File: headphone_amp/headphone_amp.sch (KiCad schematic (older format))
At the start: 40 parts, among them J1 Molex_SL_01x02_Male, J2 Molex_SL_01x02_Male, J3 Molex_SL_01x03_Male, J4 Molex_SL_01x03_Male, Q1 PZTA42, Q2 PZTA92, Q3 PZTA42, Q4 PZTA92, U1 NE5532

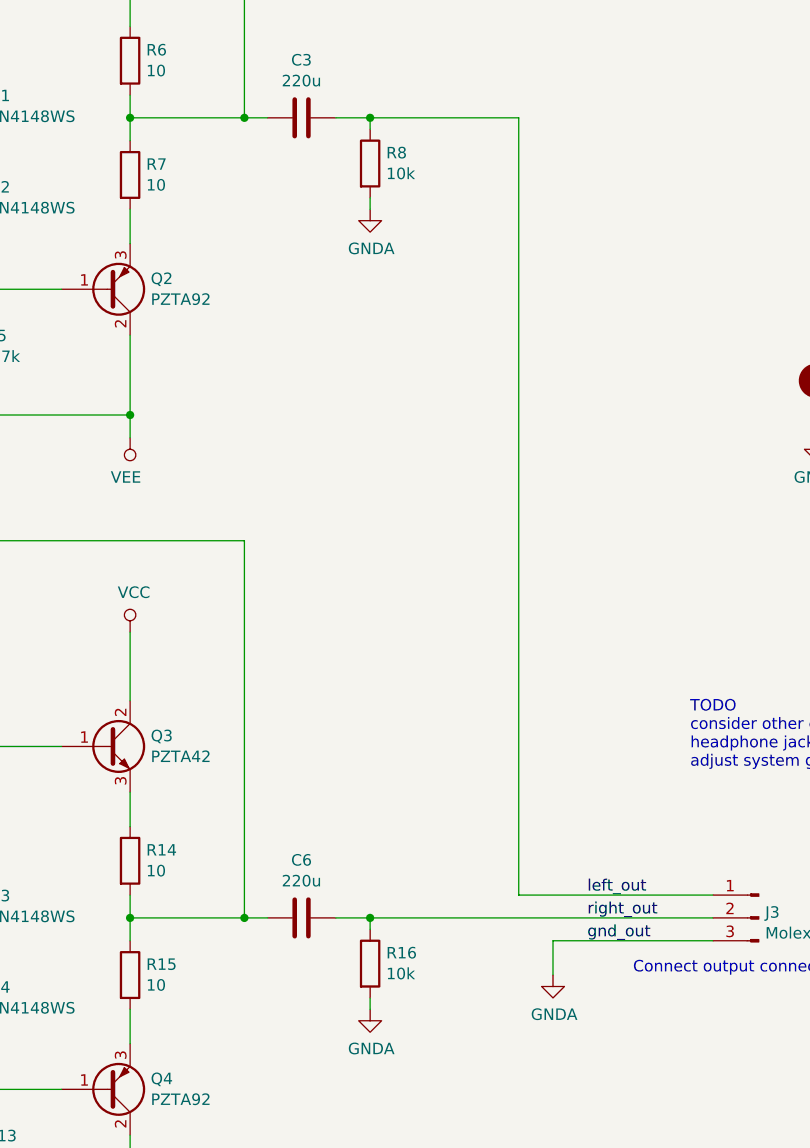
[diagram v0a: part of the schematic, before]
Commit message: update output cap footprint and bleeder resistor
- update output cap footprint (20mm height vs 25mm to match actual part)
- increase bleeder resistor value to 22k from 10k, to decrease corner
frequency
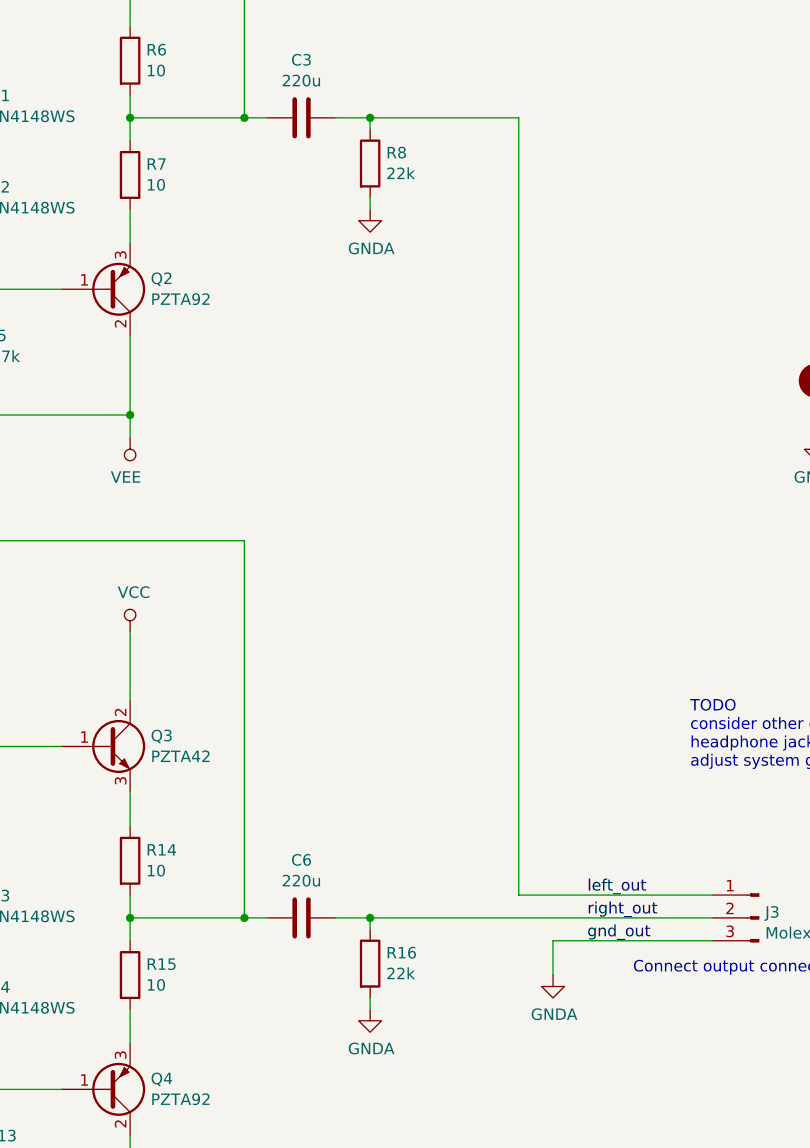
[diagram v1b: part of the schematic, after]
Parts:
- C3, C6: footprint Capacitor_THT:C_Radial_D12.5mm_H25.0mm_P5.00mm -> Capacitor_THT:C_Radial_D12.5mm_H20.0mm_P5.00mm
- R16, R8: value 10k -> 22k
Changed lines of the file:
@@
 F 0 "C3" V 5798 2550 50  0000 C CNN
 F 1 "220u" V 5889 2550 50  0000 C CNN
-F 2 "Capacitor_THT:C_Radial_D12.5mm_H25.0mm_P5.00mm" H 6088 2400 50  0001 C CNN
+F 2 "Capacitor_THT:C_Radial_D12.5mm_H20.0mm_P5.00mm" H 6088 2400 50  0001 C CNN
 F 3 "http://nichicon-us.com/english/products/pdfs/e-uvp.pdf" H 6050 2550 50  0001 C CNN
 F 4 "Nichicon" H 6050 2550 50  0001 C CNN "Manufacturer"
@@
 F 0 "C6" V 5798 6050 50  0000 C CNN
 F 1 "220u" V 5889 6050 50  0000 C CNN
-F 2 "Capacitor_THT:C_Radial_D12.5mm_H25.0mm_P5.00mm" H 6088 5900 50  0001 C CNN
+F 2 "Capacitor_THT:C_Radial_D12.5mm_H20.0mm_P5.00mm" H 6088 5900 50  0001 C CNN
 F 3 "http://nichicon-us.com/english/products/pdfs/e-uvp.pdf" H 6050 6050 50  0001 C CNN
 F 4 "Nichicon" H 6050 6050 50  0001 C CNN "Manufacturer"
@@
 P 6350 6250
 F 0 "R16" H 6420 6296 50  0000 L CNN
-F 1 "10k" H 6420 6205 50  0000 L CNN
+F 1 "22k" H 6420 6205 50  0000 L CNN
 F 2 "Resistor_SMD:R_0603_1608Metric_Pad1.05x0.95mm_HandSolder" V 6280 6250 50  0001 C CNN
 F 3 "~" H 6350 6250 50  0001 C CNN
@@
 P 6350 2750
 F 0 "R8" H 6420 2796 50  0000 L CNN
-F 1 "10k" H 6420 2705 50  0000 L CNN
+F 1 "22k" H 6420 2705 50  0000 L CNN
 F 2 "Resistor_SMD:R_0603_1608Metric_Pad1.05x0.95mm_HandSolder" V 6280 2750 50  0001 C CNN
 F 3 "~" H 6350 2750 50  0001 C CNN

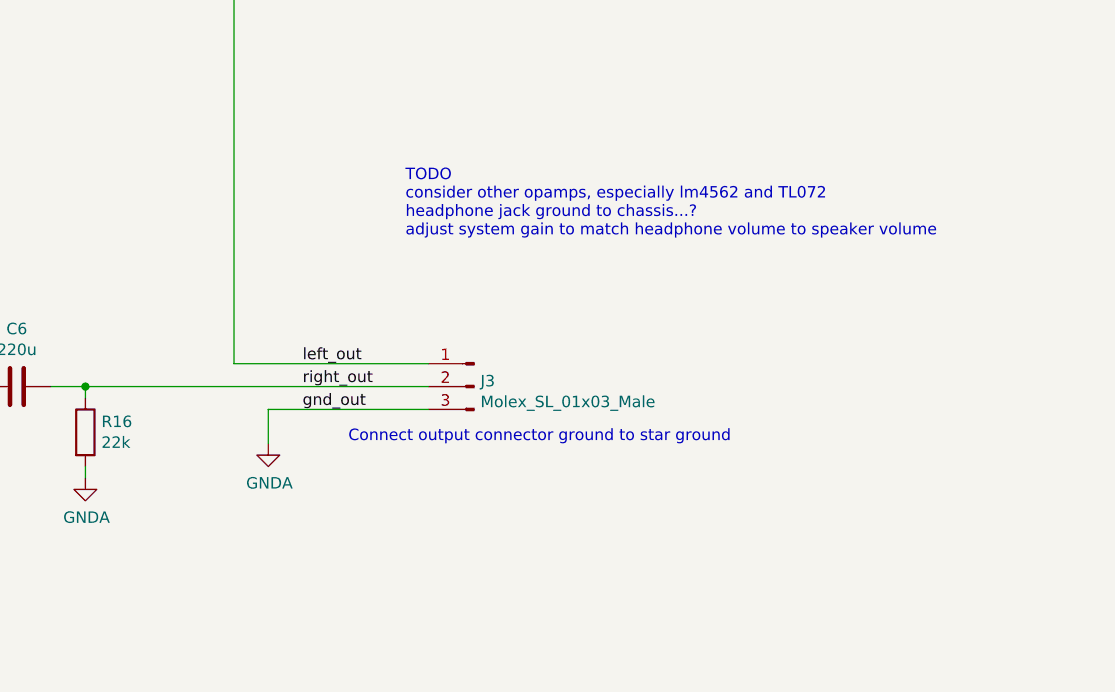
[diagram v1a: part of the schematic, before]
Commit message: connect output jack ground to star point with net tie
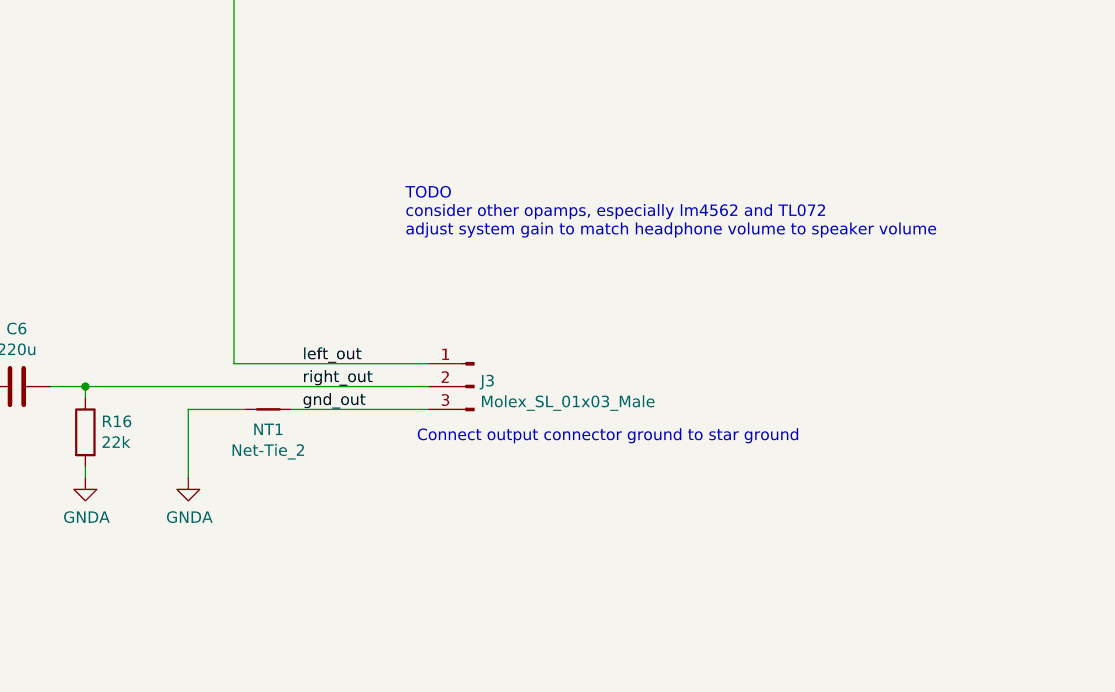
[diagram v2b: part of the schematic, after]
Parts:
- added NT1: Net-Tie_2, NetTie:NetTie-2_SMD_Pad2.0mm, symbol Device:Net-Tie_2
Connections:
- net GNDA: now also NT1.1; no longer J3.3 (Pin_3)
- new net gnd_out: J3.3 (Pin_3), NT1.2
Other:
- note added: "TODO\nconsider other opamps, especially lm4562 and TL072\nadjust system gain to match headphone volume to speaker volume"
- note removed: "TODO\nconsider other opamps, especially lm4562 and TL072\nheadphone jack ground to chassis...?\nadjust system gain to match headphone volume to speaker volume"
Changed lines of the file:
@@
 Connection ~ 1500 7350
 Text Notes 7750 5400 0    50   ~ 0
-TODO\nconsider other opamps, especially lm4562 and TL072\nheadphone jack ground to chassis...?\nadjust system gain to match headphone volume to speaker volume
+TODO\nconsider other opamps, especially lm4562 and TL072\nadjust system gain to match headphone volume to speaker volume
 $Comp
 L Connector_gkeeth:Molex_SL_01x02_Male J1
@@
 L power:GNDA #PWR0115
 U 1 1 5D92A4FE
-P 7150 6300
-F 0 "#PWR0115" H 7150 6050 50  0001 C CNN
-F 1 "GNDA" H 7155 6127 50  0000 C CNN
-F 2 "" H 7150 6300 50  0001 C CNN
-F 3 "" H 7150 6300 50  0001 C CNN
-	1    7150 6300
-	1    0    0    -1
-$EndComp
-Wire Wire Line
-	7150 6300 7150 6150
-Wire Wire Line
-	7150 6150 7850 6150
+P 6800 6450
+F 0 "#PWR0115" H 6800 6200 50  0001 C CNN
+F 1 "GNDA" H 6805 6277 50  0000 C CNN
+F 2 "" H 6800 6450 50  0001 C CNN
+F 3 "" H 6800 6450 50  0001 C CNN
+	1    6800 6450
+	1    0    0    -1
+$EndComp
 $Comp
 L Mechanical:MountingHole_Pad H1
@@
 Text Label 7300 6150 0    50   ~ 0
 gnd_out
-Text Notes 7500 6300 0    50   ~ 0
+Text Notes 7800 6300 0    50   ~ 0
 Connect output connector ground to star ground
 $Comp
@@
 $EndComp
 $Comp
-L power:GNDA #PWR?
+L power:GNDA #PWR0118
 U 1 1 5D8D030E
 P 6350 2950
-F 0 "#PWR?" H 6350 2700 50  0001 C CNN
+F 0 "#PWR0118" H 6350 2700 50  0001 C CNN
 F 1 "GNDA" H 6355 2777 50  0000 C CNN
 F 2 "" H 6350 2950 50  0001 C CNN
@@
 	6350 2550 7000 2550
 $Comp
-L power:GNDA #PWR?
+L power:GNDA #PWR0119
 U 1 1 5D8DF1C2
 P 6350 6450
-F 0 "#PWR?" H 6350 6200 50  0001 C CNN
+F 0 "#PWR0119" H 6350 6200 50  0001 C CNN
 F 1 "GNDA" H 6355 6277 50  0000 C CNN
 F 2 "" H 6350 6450 50  0001 C CNN
@@
 	1    0    0    -1
 $EndComp
+$Comp
+L Device:Net-Tie_2 NT1
+U 1 1 5D95037D
+P 7150 6150
+F 0 "NT1" H 7150 6061 50  0000 C CNN
+F 1 "Net-Tie_2" H 7150 5970 50  0000 C CNN
+F 2 "NetTie:NetTie-2_SMD_Pad2.0mm" H 7150 6150 50  0001 C CNN
+F 3 "~" H 7150 6150 50  0001 C CNN
+	1    7150 6150
+	1    0    0    -1
+$EndComp
+Wire Wire Line
+	7250 6150 7850 6150
+Wire Wire Line
+	6800 6450 6800 6150
+Wire Wire Line
+	6800 6150 7050 6150
 $EndSCHEMATC

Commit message: change to M3 mounting holes
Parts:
- H1, H2: footprint MountingHole:MountingHole_4.5mm_Pad -> MountingHole:MountingHole_3.2mm_M3_Pad
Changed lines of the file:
@@
 F 0 "H1" H 8400 3799 50  0000 L CNN
 F 1 "MountingHole_Pad" H 8400 3708 50  0000 L CNN
-F 2 "MountingHole:MountingHole_4.5mm_Pad" H 8300 3750 50  0001 C CNN
+F 2 "MountingHole:MountingHole_3.2mm_M3_Pad" H 8300 3750 50  0001 C CNN
 F 3 "~" H 8300 3750 50  0001 C CNN
 	1    8300 3750
@@
 F 0 "H2" H 9450 3799 50  0000 L CNN
 F 1 "MountingHole_Pad" H 9450 3708 50  0000 L CNN
-F 2 "MountingHole:MountingHole_4.5mm_Pad" H 9350 3750 50  0001 C CNN
+F 2 "MountingHole:MountingHole_3.2mm_M3_Pad" H 9350 3750 50  0001 C CNN
 F 3 "~" H 9350 3750 50  0001 C CNN
 	1    9350 3750

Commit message: enter all BOM info
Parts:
- C1, C2, C4, C5: Dielectric (none) -> C0G/NP0; Distributor (none) -> Mouser; Distributor PN (none) -> 80-C0603C220J5G7411; Manufacturer (none) -> KEMET; Manufacturer PN (none) -> C0603C220J5GAC7411; URL (none) -> https://www.mouser.com/ProductDetail/80-C0603C220J5G7411; Unit Price (none) -> 0.23
- D1, D2, D3, D4: Distributor (none) -> Mouser; Distributor PN (none) -> 512-1N4148WS; Manufacturer (none) -> ON Semiconductor; Manufacturer PN (none) -> 1N4148WS; URL (none) -> https://www.mouser.com/ProductDetail/512-1N4148WS; Unit Price (none) -> 0.15
- J1, J2: Distributor (none) -> Mouser; Distributor PN (none) -> 538-70553-0001; Manufacturer (none) -> Molex; Manufacturer PN (none) -> 70553-0001; URL (none) -> https://www.mouser.com/ProductDetail/538-70553-0001; Unit Price (none) -> 0.71
- J3, J4: Distributor (none) -> Mouser; Distributor PN (none) -> 538-70553-0002; Manufacturer (none) -> Molex; Manufacturer PN (none) -> 70553-0002; URL (none) -> https://www.mouser.com/ProductDetail/538-70553-0002; Unit Price (none) -> 1.12
- R1, R11, R3, R9: Distributor (none) -> Digikey; Distributor PN (none) -> YAG2321CT-ND; Manufacturer (none) -> Yageo; Manufacturer PN (none) -> RT0603FRE0710KL; URL (none) -> https://www.digikey.com/product-detail/en/yageo/RT0603FRE07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; Unit Price (none) -> 0.10
- R10, R12, R16, R2, R4, R8: Distributor (none) -> Mouser; Distributor PN (none) -> 603-RT0603FRE1322KL; Manufacturer (none) -> Yageo; Manufacturer PN (none) -> RT0603FRE1322KL; URL (none) -> https://www.mouser.com/ProductDetail/603-RT0603FRE1322KL; Unit Price (none) -> 0.19
- R13, R5: Distributor (none) -> Mouser; Distributor PN (none) -> 603-RT0603FRE074K7L; Manufacturer (none) -> Yageo; Manufacturer PN (none) -> RT0603FRE074K7L; URL (none) -> https://www.mouser.com/ProductDetail/603-RT0603FRE074K7L; Unit Price (none) -> 0.10
- U1: URL (none) -> https://www.digikey.com/products/en?keywords=NE5532AD8R2GOS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; Unit Price (none) -> 0.90
